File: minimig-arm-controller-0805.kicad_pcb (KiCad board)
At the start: 4 copper layers, 60 x 39.5 mm, 33 parts, among them J1 Conn_01x02_Male, Q1 BC807, U1 AT91SAM7S256, U2 PIC_PIN_HEADER, X1 18.342MHz

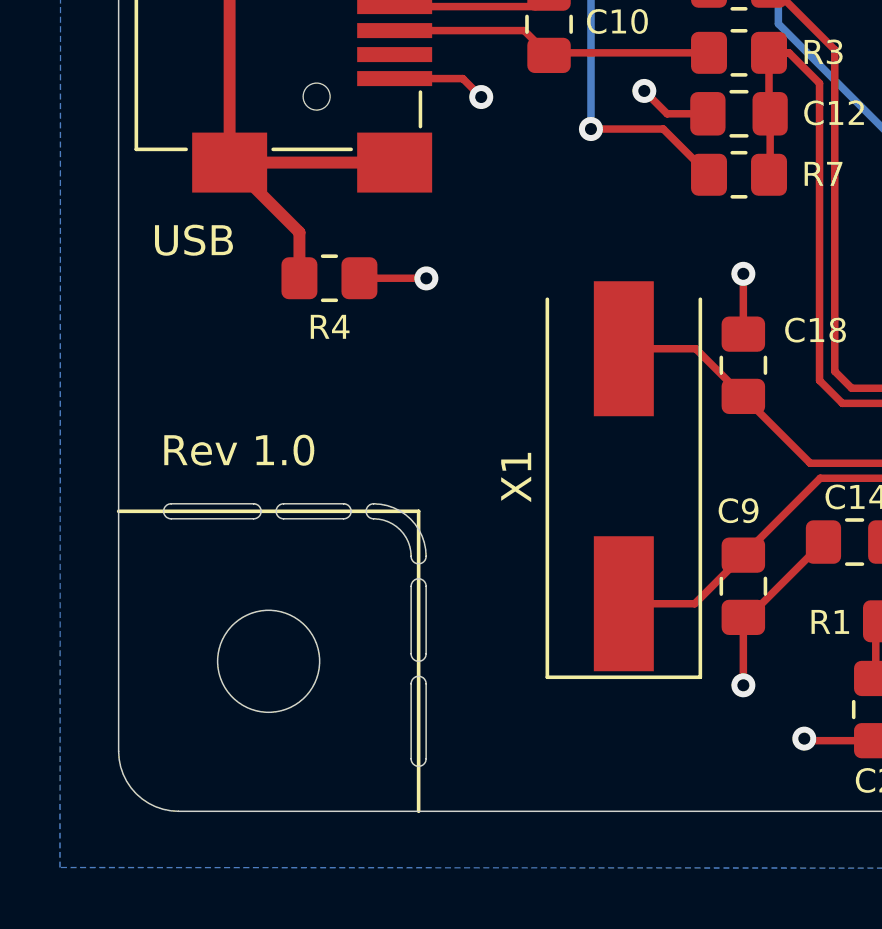
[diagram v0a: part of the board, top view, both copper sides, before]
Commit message: use handsoldering footprint for HC49-SD crystal
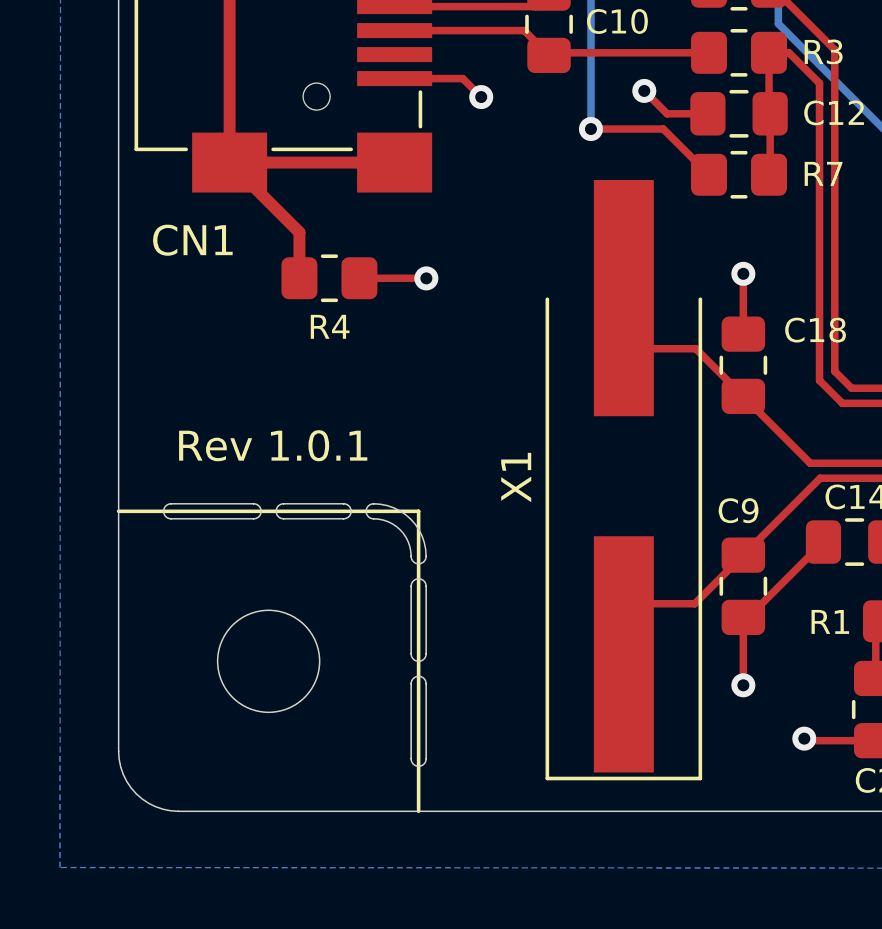
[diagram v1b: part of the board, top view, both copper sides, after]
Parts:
- X1: footprint Crystal:Crystal_SMD_HC49-SD -> Crystal:Crystal_SMD_HC49-SD_HandSoldering
- renumbered USB to CN1
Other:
- board text added: "Rev 1.0.1"
- board text removed: "Rev 1.0"
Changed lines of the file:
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@@
-(kicad_pcb (version 20171130) (host pcbnew 5.1.9-73d0e3b20d~88~ubuntu20.04.1)
+(kicad_pcb (version 20171130) (host pcbnew 5.1.10-88a1d61d58~88~ubuntu20.04.1)
   (general
     (thickness 1.6)
@@
     (add_net VDDIN)
   )
-  (module Crystal:Crystal_SMD_HC49-SD (layer F.Cu)
+  (module Crystal:Crystal_SMD_HC49-SD_HandSoldering (layer F.Cu)
     (at 116.84 48.8315 90)
-    (descr "SMD Crystal HC-49-SD http://cdn-reichelt.de/documents/datenblatt/B400/xxx-HC49-SMD.pdf, 11.4x4.7mm^2 package")
-    (tags "SMD SMT crystal")
+    (descr "SMD Crystal HC-49-SD http://cdn-reichelt.de/documents/datenblatt/B400/xxx-HC49-SMD.pdf, hand-soldering, 11.4x4.7mm^2 package")
+    (tags "SMD SMT crystal hand-soldering")
     (attr smd)
     (fp_text reference X1 (at 0 -3.55 90) (layer F.SilkS)
@@
       (effects (font (size 1 1) (thickness 0.15)))
     )
+    (fp_line (start 10.2 -2.6) (end -10.2 -2.6) (layer F.CrtYd) (width 0.05))
+    (fp_line (start 10.2 2.6) (end 10.2 -2.6) (layer F.CrtYd) (width 0.05))
+    (fp_line (start -10.2 2.6) (end 10.2 2.6) (layer F.CrtYd) (width 0.05))
+    (fp_line (start -10.2 -2.6) (end -10.2 2.6) (layer F.CrtYd) (width 0.05))
+    (fp_line (start -10.075 2.55) (end 5.9 2.55) (layer F.SilkS) (width 0.12))
+    (fp_line (start -10.075 -2.55) (end -10.075 2.55) (layer F.SilkS) (width 0.12))
+    (fp_line (start 5.9 -2.55) (end -10.075 -2.55) (layer F.SilkS) (width 0.12))
+    (fp_line (start -3.015 2.115) (end 3.015 2.115) (layer F.Fab) (width 0.1))
+    (fp_line (start -3.015 -2.115) (end 3.015 -2.115) (layer F.Fab) (width 0.1))
+    (fp_line (start 5.7 -2.35) (end -5.7 -2.35) (layer F.Fab) (width 0.1))
+    (fp_line (start 5.7 2.35) (end 5.7 -2.35) (layer F.Fab) (width 0.1))
+    (fp_line (start -5.7 2.35) (end 5.7 2.35) (layer F.Fab) (width 0.1))
     (fp_line (start -5.7 -2.35) (end -5.7 2.35) (layer F.Fab) (width 0.1))
-    (fp_line (start -5.7 2.35) (end 5.7 2.35) (layer F.Fab) (width 0.1))
-    (fp_line (start 5.7 2.35) (end 5.7 -2.35) (layer F.Fab) (width 0.1))
-    (fp_line (start 5.7 -2.35) (end -5.7 -2.35) (layer F.Fab) (width 0.1))
-    (fp_line (start -3.015 -2.115) (end 3.015 -2.115) (layer F.Fab) (width 0.1))
-    (fp_line (start -3.015 2.115) (end 3.015 2.115) (layer F.Fab) (width 0.1))
-    (fp_line (start 5.9 -2.55) (end -6.7 -2.55) (layer F.SilkS) (width 0.12))
-    (fp_line (start -6.7 -2.55) (end -6.7 2.55) (layer F.SilkS) (width 0.12))
-    (fp_line (start -6.7 2.55) (end 5.9 2.55) (layer F.SilkS) (width 0.12))
-    (fp_line (start -6.8 -2.6) (end -6.8 2.6) (layer F.CrtYd) (width 0.05))
-    (fp_line (start -6.8 2.6) (end 6.8 2.6) (layer F.CrtYd) (width 0.05))
-    (fp_line (start 6.8 2.6) (end 6.8 -2.6) (layer F.CrtYd) (width 0.05))
-    (fp_line (start 6.8 -2.6) (end -6.8 -2.6) (layer F.CrtYd) (width 0.05))
     (fp_arc (start 3.015 0) (end 3.015 -2.115) (angle 180) (layer F.Fab) (width 0.1))
     (fp_arc (start -3.015 0) (end -3.015 -2.115) (angle -180) (layer F.Fab) (width 0.1))
@@
       (effects (font (size 1 1) (thickness 0.15)))
     )
-    (pad 2 smd rect (at 4.25 0 90) (size 4.5 2) (layers F.Cu F.Paste F.Mask)
+    (pad 2 smd rect (at 5.9375 0 90) (size 7.875 2) (layers F.Cu F.Paste F.Mask)
       (net 32 "Net-(C18-Pad1)"))
-    (pad 1 smd rect (at -4.25 0 90) (size 4.5 2) (layers F.Cu F.Paste F.Mask)
+    (pad 1 smd rect (at -5.9375 0 90) (size 7.875 2) (layers F.Cu F.Paste F.Mask)
       (net 31 "Net-(C9-Pad1)"))
     (model ${KISYS3DMOD}/Crystal.3dshapes/Crystal_SMD_HC49-SD.wrl
@@
     (tags "Mini USB 2.0 Type B")
     (attr smd)
-    (fp_text reference USB (at 7.024 4.1 180) (layer F.SilkS)
+    (fp_text reference CN1 (at 7.024 4.1 180) (layer F.SilkS)
       (effects (font (size 1 1) (thickness 0.15)))
     )
@@
     )
   )
-  (gr_text "Rev 1.0" (at 104 48) (layer F.SilkS)
+  (gr_text "Rev 1.0.1" (at 105.15 47.85) (layer F.SilkS)
     (effects (font (size 1 1) (thickness 0.25)))
   )

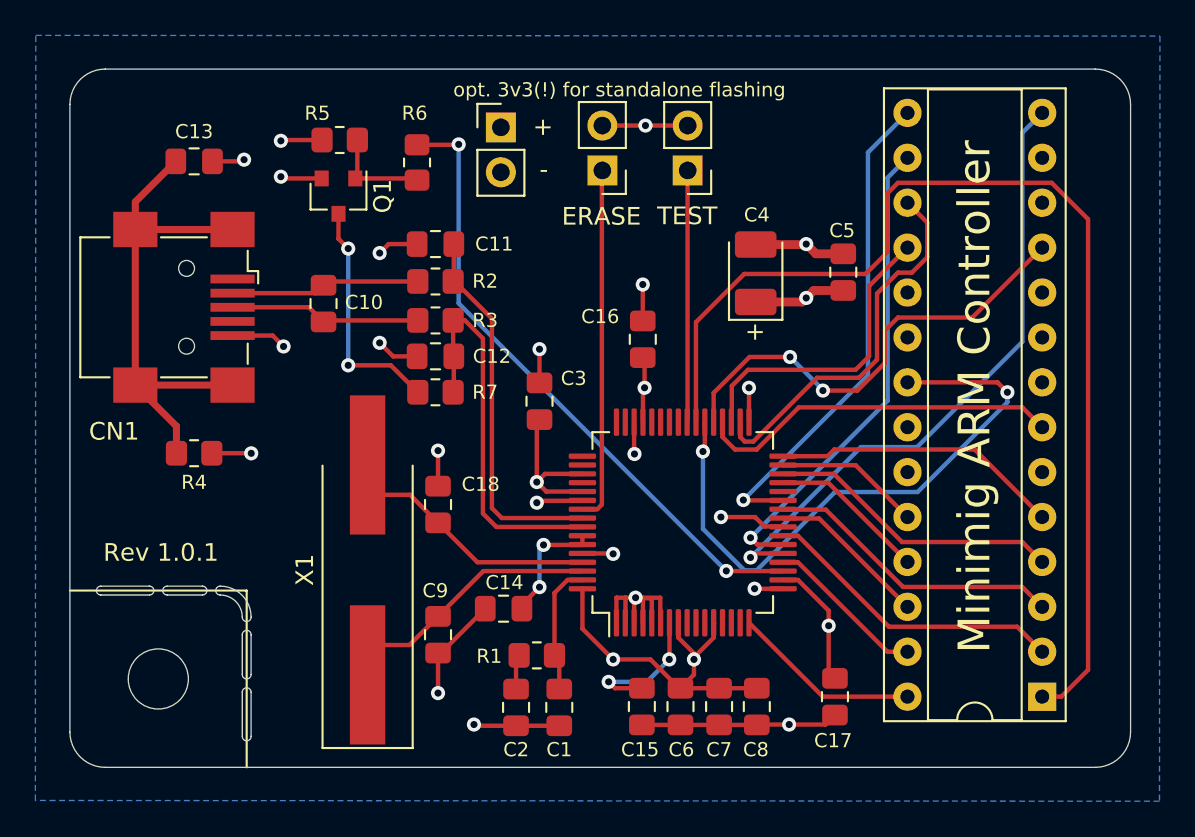
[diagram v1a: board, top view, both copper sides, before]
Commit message: rev1.0.2: some minor changes. change HC49 to THT
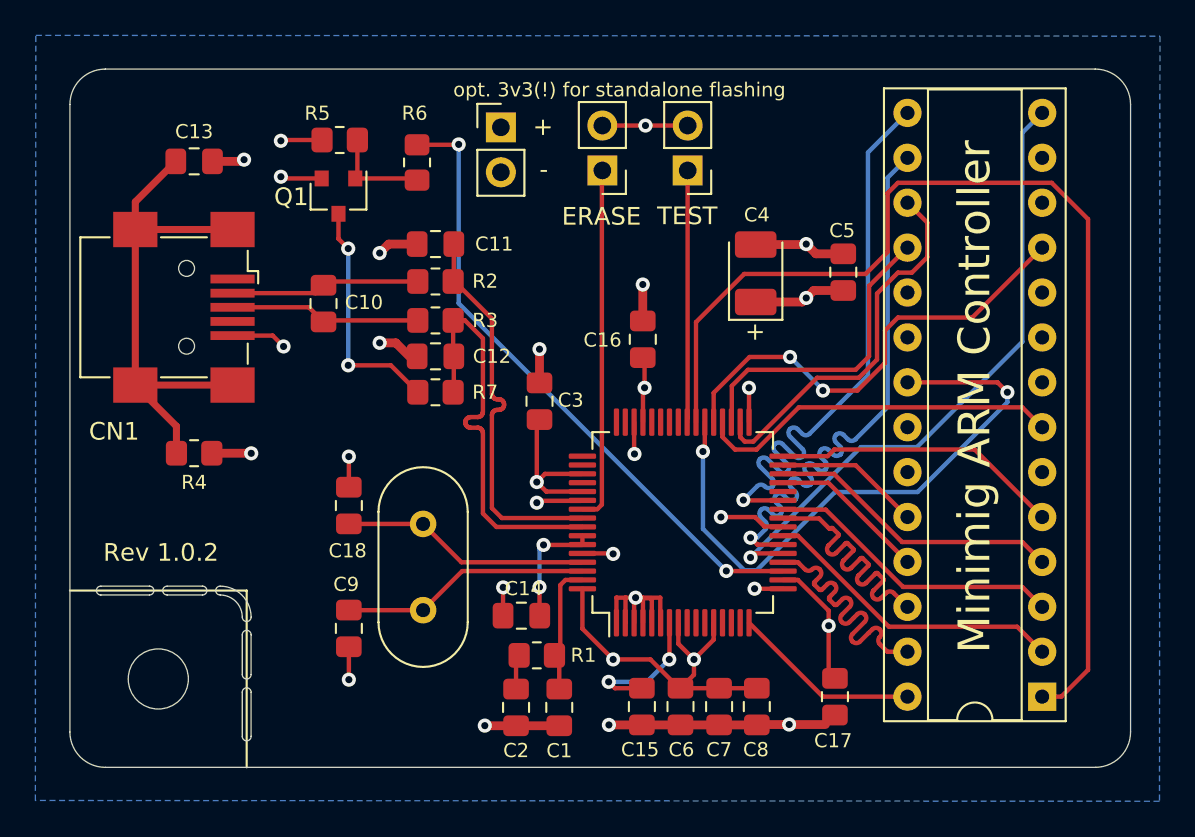
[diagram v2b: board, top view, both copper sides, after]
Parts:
- X1: footprint Crystal:Crystal_SMD_HC49-SD_HandSoldering -> Crystal:Crystal_HC49-U_Vertical
- moved C9 5.06 mm to (115.8, 52.1)
- moved C18 5.04 mm to (115.8, 45.2)
- moved X1 3.88 mm to (120.0, 51.1)
- moved C14 1.08 mm to (125.5, 51.4)
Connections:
- CN1 pad 1: (no net) -> unconnected-(CN1-Pad1)
- CN1 pad 4: (no net) -> unconnected-(CN1-Pad4)
- U1 pad 10: (no net) -> unconnected-(U1-Pad10)
- U1 pad 11: (no net) -> unconnected-(U1-Pad11)
- U1 pad 13: (no net) -> unconnected-(U1-Pad13)
- U1 pad 14: (no net) -> unconnected-(U1-Pad14)
- U1 pad 15: (no net) -> unconnected-(U1-Pad15)
- U1 pad 28: (no net) -> unconnected-(U1-Pad28)
- U1 pad 41: (no net) -> unconnected-(U1-Pad41)
- U1 pad 42: (no net) -> unconnected-(U1-Pad42)
- U1 pad 43: (no net) -> unconnected-(U1-Pad43)
- U1 pad 44: (no net) -> unconnected-(U1-Pad44)
- U1 pad 47: (no net) -> unconnected-(U1-Pad47)
- U1 pad 48: (no net) -> unconnected-(U1-Pad48)
- U1 pad 49: (no net) -> unconnected-(U1-Pad49)
- U1 pad 50: (no net) -> unconnected-(U1-Pad50)
- U1 pad 52: (no net) -> unconnected-(U1-Pad52)
- U1 pad 9: (no net) -> unconnected-(U1-Pad9)
- U2 pad 10: (no net) -> unconnected-(U2-Pad10)
- U2 pad 12: (no net) -> unconnected-(U2-Pad12)
- U2 pad 13: (no net) -> unconnected-(U2-Pad13)
- U2 pad 22: (no net) -> unconnected-(U2-Pad22)
- U2 pad 23: (no net) -> unconnected-(U2-Pad23)
- U2 pad 6: (no net) -> unconnected-(U2-Pad6)
- U2 pad 9: (no net) -> unconnected-(U2-Pad9)
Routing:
- net SDO: track 27.2 -> 35.5 mm
- net FPGA2: track 9.13 -> 16.8 mm
- net FPGA1: track 9.12 -> 16.7 mm
- net SDI: track 28.0 -> 35.6 mm
- net GND: track 62.2 -> 60.6 mm, vias 16 -> 18
- net DDP: track 22.1 -> 23.5 mm
- net DDM: track 21.3 -> 22.1 mm
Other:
- net class Default removed
- board text added: "Rev 1.0.2"
- board text removed: "Rev 1.0.1"

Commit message: rev1.0.3 reroute some stuff
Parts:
- C14, C15, C17, C3: moved to B.Cu
- moved C6 10.3 mm to (125.7, 51.4), turned to 180 degrees
- moved C14 8.81 mm to (132.9, 46.5), turned to 0 degrees
- moved C3 8.14 mm to (132.9, 44.4), turned to 0 degrees
- moved C15 7.92 mm to (132.9, 48.7), turned to 180 degrees
- moved C17 3.20 mm to (141.9, 53.1)
- moved C7 2.33 mm to (134.4, 56.6)
- moved C8 2.33 mm to (136.5, 56.6)
- moved C1 1.47 mm to (129.1, 56.5)
- moved C2 1.47 mm to (126.7, 56.5)
- moved R1 1.47 mm to (127.9, 53.6)
- moved R6 0.79 mm to (119.6, 26.6), turned to 180 degrees
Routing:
- net MCLR: track 62.6 -> 30.5 mm
- net VDDIN: track 51.7 -> 36.0 mm, vias 12 -> 10
- net VDDCORE: track 26.8 -> 16.4 mm, vias 4 -> 5
- net GND: track 60.6 -> 52.3 mm
- net ERASE: track 20.1 -> 23.3 mm
- net USB_PULLUP: track 36.0 -> 34.6 mm
- net Net-(Q1-Pad1): track 5.76 -> 4.77 mm
- net CCLK: track 20.7 -> 19.7 mm
- net DIN: track 10.7 -> 11.5 mm
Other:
- board text added: "Rev 1.0.3"
- board text removed: "Rev 1.0.2"
